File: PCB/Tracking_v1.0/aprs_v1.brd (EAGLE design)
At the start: 61 x 61 mm, 24 parts, among them IC1 ATMEGA328PB-AU, X1 BU-SMA-V

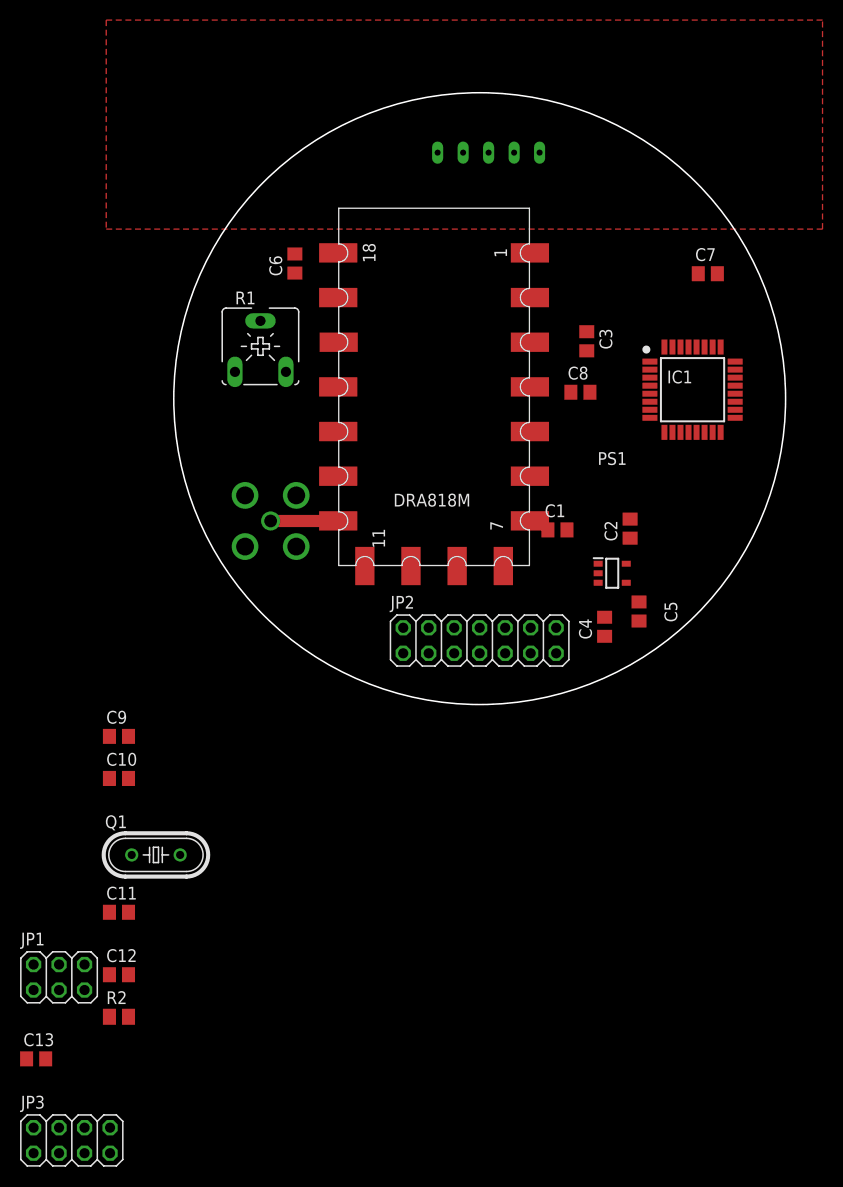
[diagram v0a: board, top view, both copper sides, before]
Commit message: single side routing
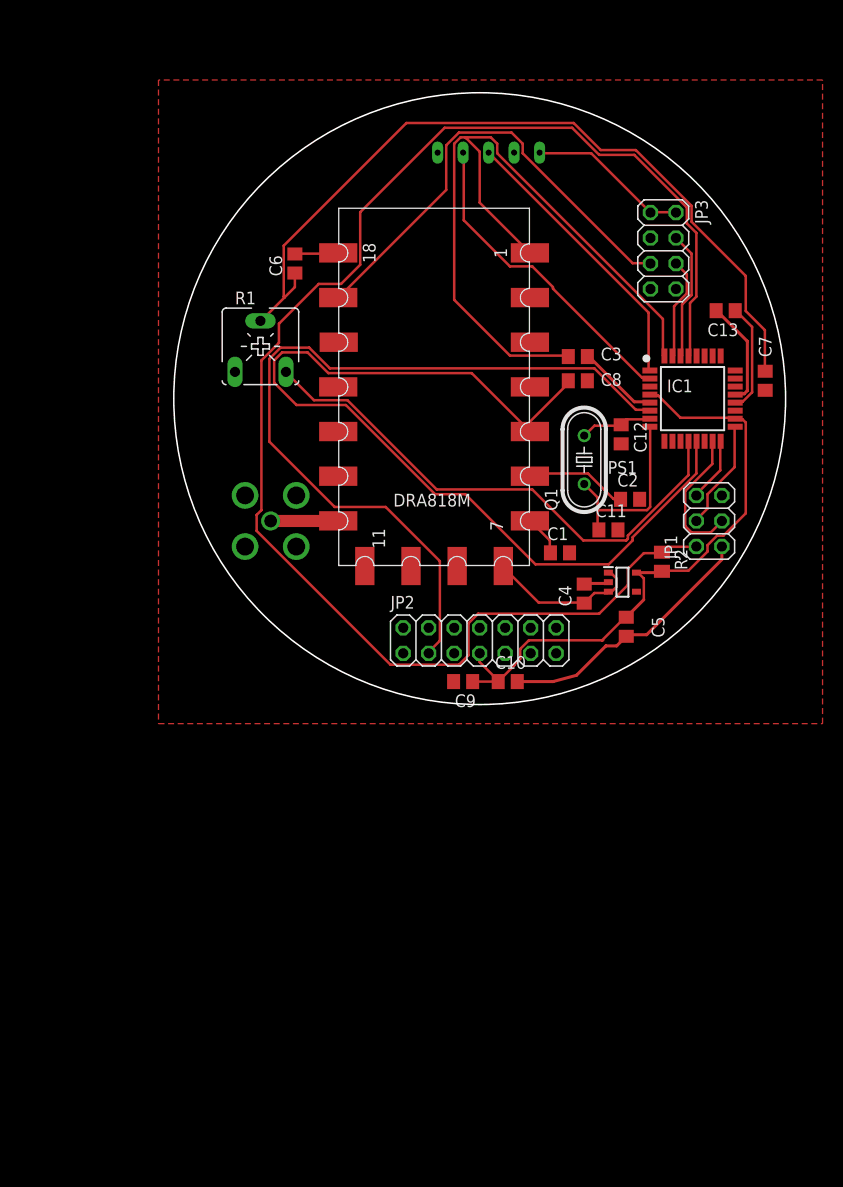
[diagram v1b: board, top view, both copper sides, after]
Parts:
- moved JP3 106.4 mm to (48.8, 45.2), turned to 270 degrees
- moved C13 101.4 mm to (55.0, 39.2), turned to 180 degrees
- moved JP1 79.1 mm to (53.3, 18.3), turned to 90 degrees
- moved C12 73.5 mm to (44.6, 26.9), turned to 270 degrees
- moved R2 70.6 mm to (48.6, 14.2), turned to 270 degrees
- moved C11 61.9 mm to (43.3, 17.4)
- moved Q1 58.1 mm to (40.9, 24.4), turned to 90 degrees
- moved C10 39.9 mm to (33.3, 2.29)
- moved C9 34.7 mm to (28.8, 2.29), turned to 180 degrees
- moved C7 12.1 mm to (58.9, 32.3), turned to 270 degrees
- moved C4 3.88 mm to (40.9, 11.0)
- moved C2 2.92 mm to (45.5, 20.4), turned to 0 degrees
- moved C1 2.30 mm to (38.5, 15.1)
- moved C5 1.98 mm to (45.1, 7.75)
- moved C3 1.76 mm to (40.3, 34.7), turned to 0 degrees
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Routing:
- net RESET: track 0.00 -> 149.2 mm
- net MC_PPT: track 0.00 -> 95.0 mm
- net I2C_SCL: track 0.00 -> 80.8 mm
- net N$7: track 0.00 -> 80.0 mm
- net SQL: track 0.00 -> 76.3 mm
- net V_3.3: track 0.00 -> 61.4 mm
- net MC_APRS_OUT: track 0.00 -> 53.3 mm
- net GND: track 0.00 -> 47.9 mm
- net MU_RX_1: track 0.00 -> 46.5 mm
- net MU_RX_2: track 0.00 -> 31.9 mm
- net VBAT_OUT: track 0.00 -> 31.6 mm
- net MU_TX_2: track 0.00 -> 28.4 mm
- net N$9: track 0.00 -> 18.6 mm
- net MOSI: track 0.00 -> 14.0 mm
- net RX0: track 0.00 -> 12.9 mm
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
